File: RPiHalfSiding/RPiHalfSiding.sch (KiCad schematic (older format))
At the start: 9 parts, among them J0 RPi_GPIO, T3 12 to 15V, T4 Motor 0, T5 Motor 1, U4 TC4428, U5 TC4428, U6 74HC00

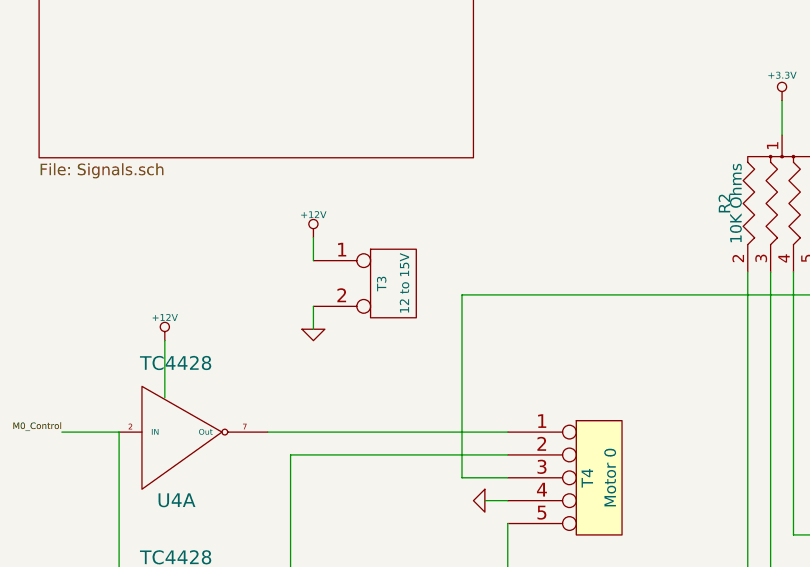
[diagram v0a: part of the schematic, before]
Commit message: Final Silktweaks for RPiHalfSiding
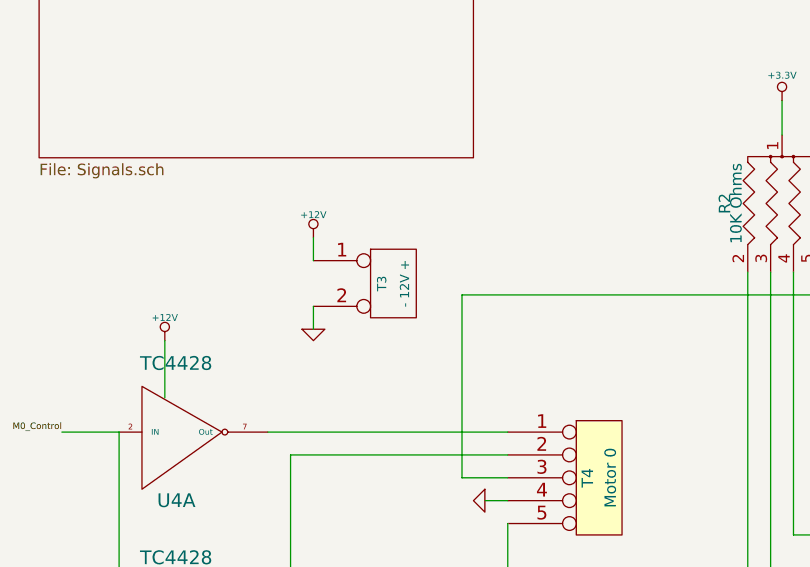
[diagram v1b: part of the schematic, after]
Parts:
- T3: value 12 to 15V -> - 12V +
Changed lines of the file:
@@
 Sheet 1 3
 Title ""
-Date "8 oct 2018"
+Date "20 oct 2018"
 Rev ""
 Comp ""
@@
 P 5800 3600
 F 0 "T3" V 5750 3600 40  0000 C CNN
-F 1 "12 to 15V" V 5850 3600 40  0000 C CNN
+F 1 "- 12V +" V 5850 3600 40  0000 C CNN
 F 2 "~" H 5800 3600 60  0000 C CNN
 F 3 "~" H 5800 3600 60  0000 C CNN
